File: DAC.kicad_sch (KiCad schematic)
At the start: 0 parts

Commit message: Connected FPGA and DAC
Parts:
- added C64, C65, C66, C67: 10u, symbol Device:C_Polarized_US
- added U8: ~, symbol GuitarZero:PCM1754
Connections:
- new net: C66.1, U8.7 (VoutL)
- new net: C67.1, U8.8 (VoutR)
- new net: C64.1, U8.10 (Vcom)
- new net +5V: C65.1, U8.6 (VCC)
- new net BIT_CLOCK: U8.1 (BCK)
- new net DATA_INN: U8.2 (DATA)
- new net GND: C64.2, C65.2, U8.12 (TEST), U8.13 (DEMP), U8.14 (MUTE), U8.15 (FMT), U8.4 (DGND), U8.9 (AGND)
- new net LEFT_RIGHT_CLOCK: U8.3 (LRCK)
- new net OUT_LEFT: C66.2
- new net OUT_RIGHT: C67.2
- new net SYSTEM_CLOCK_INPUT: U8.16 (SCK)
- no-connect marks 0 -> 2
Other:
- note added: "Theese could be used But would require aditional logic And should be done in the FPGA if needed"

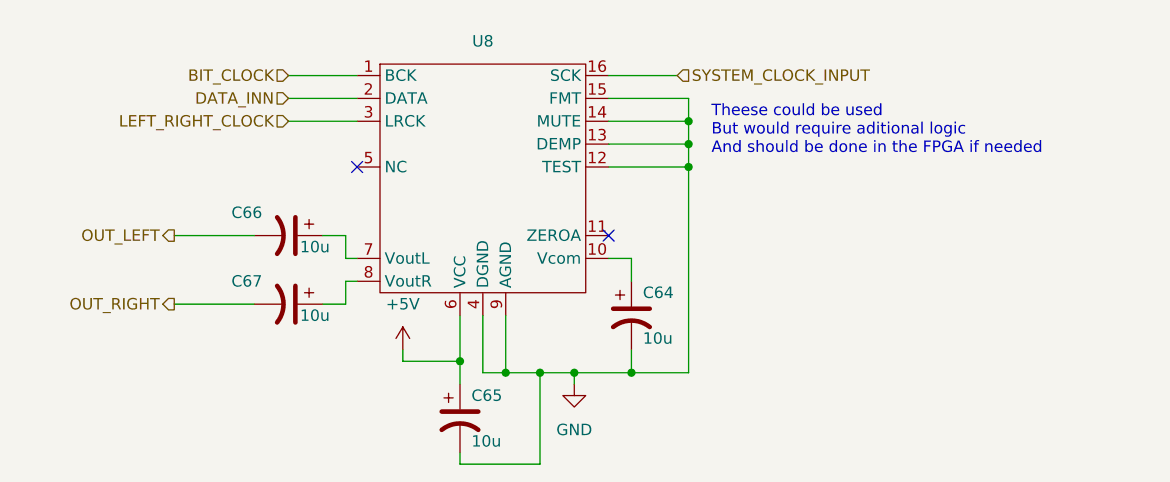
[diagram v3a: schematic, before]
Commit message: Now follows with Electrical Rules
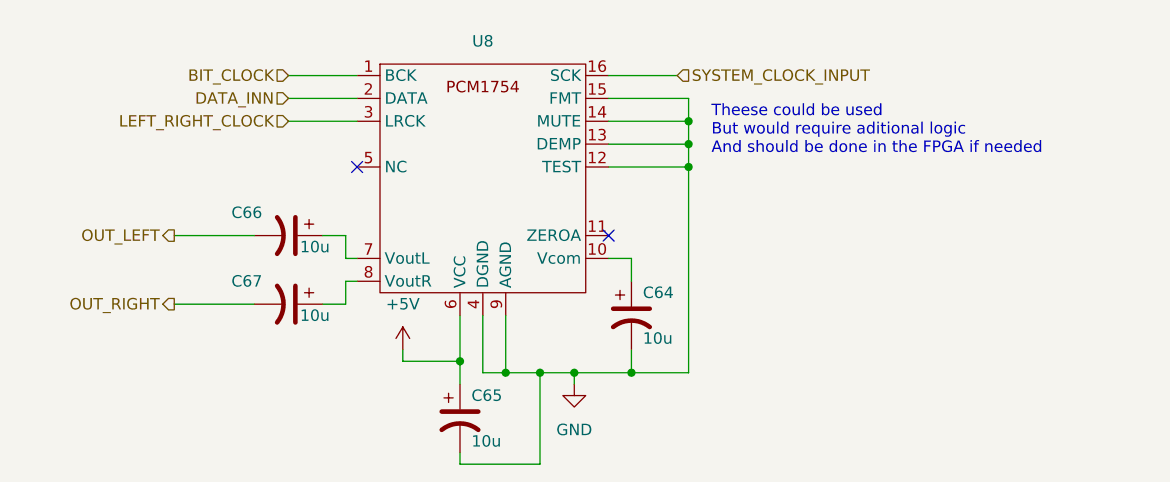
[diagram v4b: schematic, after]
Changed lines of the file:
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@@
     (effects (font (size 1.27 1.27)) (justify left))
+  )
+  (symbol (lib_id "GuitarZero:PCM1754") (at 125.73 92.71 0) (unit 1)
+    (in_bom yes) (on_board yes) (dnp no) (fields_autoplaced)
+    (property "Reference" "U8" (at 125.73 78.74 0)
+      (effects (font (size 1.27 1.27)))
+    )
+    (property "Value" "~" (at 118.11 85.09 0)
+      (effects (font (size 1.27 1.27)))
+    )
+    (property "Footprint" "" (at 118.11 85.09 0)
+      (effects (font (size 1.27 1.27)) hide)
+    )
+    (property "Datasheet" "" (at 118.11 85.09 0)
+      (effects (font (size 1.27 1.27)) hide)
+    )
+    (pin "1")
+    (pin "10")
+    (pin "11")
+    (pin "12")
+    (pin "13")
+    (pin "14")
+    (pin "15")
+    (pin "16")
+    (pin "2")
+    (pin "3")
+    (pin "4")
+    (pin "5")
+    (pin "6")
+    (pin "7")
+    (pin "8")
+    (pin "9")
+    (instances
+      (project "GuitarZero"
+        (path "/fba50eda-8593-4456-af98-ff56fd418a76/17583736-1e43-4d1e-aeda-75c9cd3f21c5"
+          (reference "U8") (unit 1)
+        )
+      )
+    )
   )
   (symbol (lib_id "Device:C_Polarized_US") (at 104.14 100.33 270) (unit 1)
@@
         )
       )
-    )
-  )
-  (symbol (lib_id "GuitarZero:PCM1754") (at 118.11 85.09 0) (unit 1)
-    (in_bom yes) (on_board yes) (dnp no) (fields_autoplaced)
-    (property "Reference" "U8" (at 125.73 78.74 0)
-      (effects (font (size 1.27 1.27)))
-    )
-    (property "Value" "~" (at 118.11 85.09 0)
-      (effects (font (size 1.27 1.27)))
-    )
-    (property "Footprint" "" (at 118.11 85.09 0)
-      (effects (font (size 1.27 1.27)) hide)
-    )
-    (property "Datasheet" "" (at 118.11 85.09 0)
-      (effects (font (size 1.27 1.27)) hide)
-    )
-    (pin "1")
-    (pin "10")
-    (pin "11")
-    (pin "12")
-    (pin "13")
-    (pin "14")
-    (pin "15")
-    (pin "16")
-    (pin "2")
-    (pin "3")
-    (pin "4")
-    (pin "5")
-    (pin "6")
-    (pin "7")
-    (pin "8")
-    (pin "9")
-    (instances
-      (project "GuitarZero"
-        (path "/fba50eda-8593-4456-af98-ff56fd418a76/17583736-1e43-4d1e-aeda-75c9cd3f21c5"
-          (reference "U8") (unit 1)
-        )
-      )

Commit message: Added Anti-noise resistors to DAC
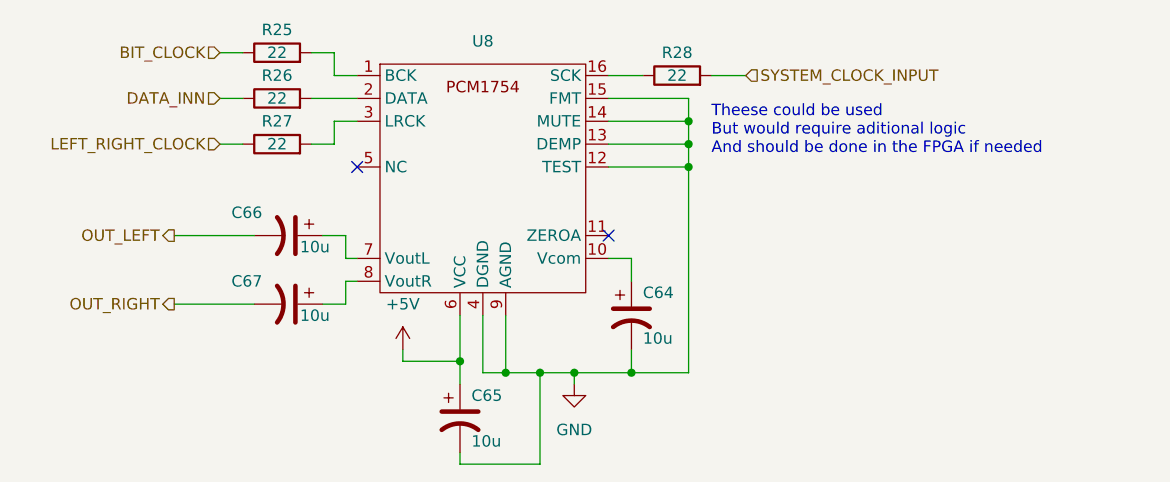
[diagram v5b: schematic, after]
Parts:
- added R25, R26, R27, R28: 22, symbol Device:R
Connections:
- net BIT_CLOCK: now also R25.1; no longer U8.1 (BCK)
- net DATA_INN: now also R26.1; no longer U8.2 (DATA)
- net LEFT_RIGHT_CLOCK: now also R27.1; no longer U8.3 (LRCK)
- net SYSTEM_CLOCK_INPUT: now also R28.2; no longer U8.16 (SCK)
- new net: R25.2, U8.1 (BCK)
- new net: R28.1, U8.16 (SCK)
- new net: R26.2, U8.2 (DATA)
- new net: R27.2, U8.3 (LRCK)
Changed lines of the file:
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@@
-    (stroke (width 0) (type default))
-  )
-  (wire (pts (xy 104.14 85.09) (xy 111.76 85.09))
     (stroke (width 0) (type default))
   )
@@
     (stroke (width 0) (type default))
   )
+  (wire (pts (xy 109.22 80.01) (xy 109.22 82.55))
+    (stroke (width 0) (type default))
+  )
   (wire (pts (xy 132.08 125.73) (xy 132.08 115.57))
     (stroke (width 0) (type default))
   )
+  (wire (pts (xy 96.52 80.01) (xy 99.06 80.01))
+    (stroke (width 0) (type default))
+  )
   (wire (pts (xy 148.59 115.57) (xy 142.24 115.57))
     (stroke (width 0) (type default))
@@
     (stroke (width 0) (type default))
   )
+  (wire (pts (xy 106.68 90.17) (xy 109.22 90.17))
+    (stroke (width 0) (type default))
+  )
+  (wire (pts (xy 139.7 82.55) (xy 143.51 82.55))
+    (stroke (width 0) (type default))
+  )
   (wire (pts (xy 139.7 90.17) (xy 148.59 90.17))
     (stroke (width 0) (type default))
   )
+  (wire (pts (xy 109.22 90.17) (xy 109.22 87.63))
+    (stroke (width 0) (type default))
+  )
   (wire (pts (xy 148.59 90.17) (xy 148.59 92.71))
     (stroke (width 0) (type default))
@@
     (stroke (width 0) (type default))
   )
-  (wire (pts (xy 104.14 82.55) (xy 111.76 82.55))
-    (stroke (width 0) (type default))
-  )
   (wire (pts (xy 148.59 87.63) (xy 148.59 90.17))
     (stroke (width 0) (type default))
   )
+  (wire (pts (xy 106.68 85.09) (xy 111.76 85.09))
+    (stroke (width 0) (type default))
+  )
   (wire (pts (xy 128.27 115.57) (xy 132.08 115.57))
     (stroke (width 0) (type default))
@@
     (stroke (width 0) (type default))
   )
+  (wire (pts (xy 109.22 82.55) (xy 111.76 82.55))
+    (stroke (width 0) (type default))
+  )
   (wire (pts (xy 142.24 102.87) (xy 139.7 102.87))
     (stroke (width 0) (type default))
@@
     (stroke (width 0) (type default))
   )
-  (wire (pts (xy 139.7 82.55) (xy 147.32 82.55))
-    (stroke (width 0) (type default))
-  )
   (wire (pts (xy 128.27 109.22) (xy 128.27 115.57))
     (stroke (width 0) (type default))
@@
     (stroke (width 0) (type default))
   )
+  (wire (pts (xy 109.22 87.63) (xy 111.76 87.63))
+    (stroke (width 0) (type default))
+  )
   (wire (pts (xy 91.44 107.95) (xy 100.33 107.95))
     (stroke (width 0) (type default))
@@
     (stroke (width 0) (type default))
   )
+  (wire (pts (xy 106.68 80.01) (xy 109.22 80.01))
+    (stroke (width 0) (type default))
+  )
+  (wire (pts (xy 96.52 85.09) (xy 99.06 85.09))
+    (stroke (width 0) (type default))
+  )
   (wire (pts (xy 123.19 109.22) (xy 123.19 114.3))
     (stroke (width 0) (type default))
   )
-  (wire (pts (xy 104.14 87.63) (xy 111.76 87.63))
+  (wire (pts (xy 96.52 90.17) (xy 99.06 90.17))
     (stroke (width 0) (type default))
   )
@@
   )
   (wire (pts (xy 110.49 105.41) (xy 110.49 107.95))
+    (stroke (width 0) (type default))
+  )
+  (wire (pts (xy 151.13 82.55) (xy 154.94 82.55))
     (stroke (width 0) (type default))
   )
@@
     (effects (font (size 1.27 1.27)) (justify left bottom))
   )
-  (hierarchical_label "LEFT_RIGHT_CLOCK" (shape input) (at 104.14 87.63 180) (fields_autoplaced)
+  (hierarchical_label "LEFT_RIGHT_CLOCK" (shape input) (at 96.52 90.17 180) (fields_autoplaced)
     (effects (font (size 1.27 1.27)) (justify right))
   )
@@
     (effects (font (size 1.27 1.27)) (justify right))
   )
-  (hierarchical_label "DATA_INN" (shape input) (at 104.14 85.09 180) (fields_autoplaced)
+  (hierarchical_label "DATA_INN" (shape input) (at 96.52 85.09 180) (fields_autoplaced)
     (effects (font (size 1.27 1.27)) (justify right))
   )
@@
     (effects (font (size 1.27 1.27)) (justify right))
   )
-  (hierarchical_label "BIT_CLOCK" (shape input) (at 104.14 82.55 180) (fields_autoplaced)
+  (hierarchical_label "BIT_CLOCK" (shape input) (at 96.52 80.01 180) (fields_autoplaced)
     (effects (font (size 1.27 1.27)) (justify right))
   )
-  (hierarchical_label "SYSTEM_CLOCK_INPUT" (shape input) (at 147.32 82.55 0) (fields_autoplaced)
+  (hierarchical_label "SYSTEM_CLOCK_INPUT" (shape input) (at 154.94 82.55 0) (fields_autoplaced)
     (effects (font (size 1.27 1.27)) (justify left))
+  )
+  (symbol (lib_id "Device:R") (at 102.87 80.01 90) (unit 1)
+    (in_bom yes) (on_board yes) (dnp no)
+    (property "Reference" "R25" (at 102.87 77.47 90)
+      (effects (font (size 1.27 1.27)))
+    )
+    (property "Value" "22" (at 102.87 80.01 90)
+      (effects (font (size 1.27 1.27)))
+    )
+    (property "Footprint" "" (at 102.87 81.788 90)
+      (effects (font (size 1.27 1.27)) hide)
+    )
+    (property "Datasheet" "~" (at 102.87 80.01 0)
+      (effects (font (size 1.27 1.27)) hide)
+    )
+    (pin "1")
+    (pin "2")
+    (instances
+      (project "GuitarZero"
+        (path "/fba50eda-8593-4456-af98-ff56fd418a76/17583736-1e43-4d1e-aeda-75c9cd3f21c5"
+          (reference "R25") (unit 1)
+        )
+      )
+    )
   )
   (symbol (lib_id "GuitarZero:PCM1754") (at 125.73 92.71 0) (unit 1)
@@
     )
   )
+  (symbol (lib_id "Device:R") (at 147.32 82.55 90) (unit 1)
+    (in_bom yes) (on_board yes) (dnp no)
+    (property "Reference" "R28" (at 147.32 80.01 90)
+      (effects (font (size 1.27 1.27)))
+    )
+    (property "Value" "22" (at 147.32 82.55 90)
+      (effects (font (size 1.27 1.27)))
+    )
+    (property "Footprint" "" (at 147.32 84.328 90)
+      (effects (font (size 1.27 1.27)) hide)
+    )
+    (property "Datasheet" "~" (at 147.32 82.55 0)
+      (effects (font (size 1.27 1.27)) hide)
+    )
+    (pin "1")
+    (pin "2")
+    (instances
+      (project "GuitarZero"
+        (path "/fba50eda-8593-4456-af98-ff56fd418a76/17583736-1e43-4d1e-aeda-75c9cd3f21c5"
+          (reference "R28") (unit 1)
+        )
+      )
+    )
+  )
+  (symbol (lib_id "Device:R") (at 102.87 85.09 90) (unit 1)
+    (in_bom yes) (on_board yes) (dnp no)
+    (property "Reference" "R26" (at 102.87 82.55 90)
+      (effects (font (size 1.27 1.27)))
+    )
+    (property "Value" "22" (at 102.87 85.09 90)
+      (effects (font (size 1.27 1.27)))
+    )
+    (property "Footprint" "" (at 102.87 86.868 90)
+      (effects (font (size 1.27 1.27)) hide)
+    )
+    (property "Datasheet" "~" (at 102.87 85.09 0)
+      (effects (font (size 1.27 1.27)) hide)
+    )
+    (pin "1")
+    (pin "2")
+    (instances
+      (project "GuitarZero"
+        (path "/fba50eda-8593-4456-af98-ff56fd418a76/17583736-1e43-4d1e-aeda-75c9cd3f21c5"
+          (reference "R26") (unit 1)
+        )
+      )
+    )
+  )
   (symbol (lib_id "Device:C_Polarized_US") (at 142.24 109.22 0) (unit 1)
     (in_bom yes) (on_board yes) (dnp no)
@@
         )
       )
+    )
+  )
+  (symbol (lib_id "Device:R") (at 102.87 90.17 90) (unit 1)
+    (in_bom yes) (on_board yes) (dnp no)
+    (property "Reference" "R27" (at 102.87 87.63 90)
+      (effects (font (size 1.27 1.27)))
+    )
+    (property "Value" "22" (at 102.87 90.17 90)
+      (effects (font (size 1.27 1.27)))
+    )
+    (property "Footprint" "" (at 102.87 91.948 90)
+      (effects (font (size 1.27 1.27)) hide)
+    )
+    (property "Datasheet" "~" (at 102.87 90.17 0)
+      (effects (font (size 1.27 1.27)) hide)
+    )
+    (pin "1")
+    (pin "2")
+    (instances
+      (project "GuitarZero"
+        (path "/fba50eda-8593-4456-af98-ff56fd418a76/17583736-1e43-4d1e-aeda-75c9cd3f21c5"
+          (reference "R27") (unit 1)
+        )
+      )

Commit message: Added footprints to symbols
Some nice light work
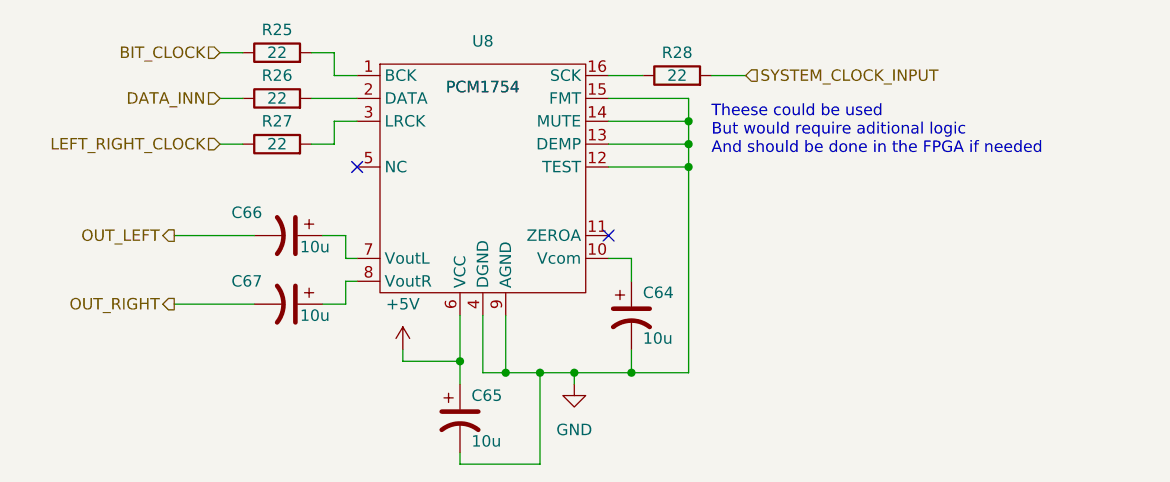
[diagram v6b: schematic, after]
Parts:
- C64, C65, C66, C67: footprint (none) -> Capacitor_SMD:C_1206_3216Metric
- R25, R26, R27, R28: footprint (none) -> Resistor_SMD:R_1206_3216Metric
- U8: value ~ -> PCM1754; footprint (none) -> PCM1754DBQR:SOP63P599X175-16N
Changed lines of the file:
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@@
       (effects (font (size 1.27 1.27)))
     )
-    (property "Footprint" "" (at 102.87 81.788 90)
+    (property "Footprint" "Resistor_SMD:R_1206_3216Metric" (at 102.87 81.788 90)
       (effects (font (size 1.27 1.27)) hide)
     )
@@
   )
   (symbol (lib_id "GuitarZero:PCM1754") (at 125.73 92.71 0) (unit 1)
-    (in_bom yes) (on_board yes) (dnp no) (fields_autoplaced)
+    (in_bom yes) (on_board yes) (dnp no)
     (property "Reference" "U8" (at 125.73 78.74 0)
       (effects (font (size 1.27 1.27)))
     )
-    (property "Value" "~" (at 118.11 85.09 0)
-      (effects (font (size 1.27 1.27)))
-    )
-    (property "Footprint" "" (at 118.11 85.09 0)
+    (property "Value" "PCM1754" (at 125.73 83.82 0)
+      (effects (font (size 1.27 1.27)))
+    )
+    (property "Footprint" "PCM1754DBQR:SOP63P599X175-16N" (at 118.11 85.09 0)
       (effects (font (size 1.27 1.27)) hide)
     )
@@
       (effects (font (size 1.27 1.27)) (justify left))
     )
-    (property "Footprint" "" (at 104.14 100.33 0)
+    (property "Footprint" "Capacitor_SMD:C_1206_3216Metric" (at 104.14 100.33 0)
       (effects (font (size 1.27 1.27)) hide)
     )
@@
       (effects (font (size 1.27 1.27)) (justify left))
     )
-    (property "Footprint" "" (at 104.14 107.95 0)
+    (property "Footprint" "Capacitor_SMD:C_1206_3216Metric" (at 104.14 107.95 0)
       (effects (font (size 1.27 1.27)) hide)
     )
@@
       (effects (font (size 1.27 1.27)))
     )
-    (property "Footprint" "" (at 147.32 84.328 90)
+    (property "Footprint" "Resistor_SMD:R_1206_3216Metric" (at 147.32 84.328 90)
       (effects (font (size 1.27 1.27)) hide)
     )
@@
       (effects (font (size 1.27 1.27)))
     )
-    (property "Footprint" "" (at 102.87 86.868 90)
+    (property "Footprint" "Resistor_SMD:R_1206_3216Metric" (at 102.87 86.868 90)
       (effects (font (size 1.27 1.27)) hide)
     )
@@
       (effects (font (size 1.27 1.27)) (justify left))
     )
-    (property "Footprint" "" (at 142.24 109.22 0)
+    (property "Footprint" "Capacitor_SMD:C_1206_3216Metric" (at 142.24 109.22 0)
       (effects (font (size 1.27 1.27)) hide)
     )
@@
       (effects (font (size 1.27 1.27)))
     )
-    (property "Footprint" "" (at 102.87 91.948 90)
+    (property "Footprint" "Resistor_SMD:R_1206_3216Metric" (at 102.87 91.948 90)
       (effects (font (size 1.27 1.27)) hide)
     )
@@
       (effects (font (size 1.27 1.27)) (justify left))
     )
-    (property "Footprint" "" (at 123.19 120.65 0)
-      (effects (font (size 1.27 1.27)) hide)
-    )
+    (property "Footprint" "Capacitor_SMD:C_1206_3216Metric" (at 123.19 120.65 0)
+      (effects (font (size 1.27 1.27)) hide)
+    )

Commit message: Changed Reistor and Capacitor size fomr 1206 to 0805
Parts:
- C64, C65, C66, C67: footprint Capacitor_SMD:C_1206_3216Metric -> Capacitor_SMD:C_0805_2012Metric
- R25, R26, R27, R28: footprint Resistor_SMD:R_1206_3216Metric -> Resistor_SMD:R_0805_2012Metric
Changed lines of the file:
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@@
       (effects (font (size 1.27 1.27)))
     )
-    (property "Footprint" "Resistor_SMD:R_1206_3216Metric" (at 102.87 81.788 90)
+    (property "Footprint" "Resistor_SMD:R_0805_2012Metric" (at 102.87 81.788 90)
       (effects (font (size 1.27 1.27)) hide)
     )
@@
       (effects (font (size 1.27 1.27)) (justify left))
     )
-    (property "Footprint" "Capacitor_SMD:C_1206_3216Metric" (at 104.14 100.33 0)
+    (property "Footprint" "Capacitor_SMD:C_0805_2012Metric" (at 104.14 100.33 0)
       (effects (font (size 1.27 1.27)) hide)
     )
@@
       (effects (font (size 1.27 1.27)) (justify left))
     )
-    (property "Footprint" "Capacitor_SMD:C_1206_3216Metric" (at 104.14 107.95 0)
+    (property "Footprint" "Capacitor_SMD:C_0805_2012Metric" (at 104.14 107.95 0)
       (effects (font (size 1.27 1.27)) hide)
     )
@@
       (effects (font (size 1.27 1.27)))
     )
-    (property "Footprint" "Resistor_SMD:R_1206_3216Metric" (at 147.32 84.328 90)
+    (property "Footprint" "Resistor_SMD:R_0805_2012Metric" (at 147.32 84.328 90)
       (effects (font (size 1.27 1.27)) hide)
     )
@@
       (effects (font (size 1.27 1.27)))
     )
-    (property "Footprint" "Resistor_SMD:R_1206_3216Metric" (at 102.87 86.868 90)
+    (property "Footprint" "Resistor_SMD:R_0805_2012Metric" (at 102.87 86.868 90)
       (effects (font (size 1.27 1.27)) hide)
     )
@@
       (effects (font (size 1.27 1.27)) (justify left))
     )
-    (property "Footprint" "Capacitor_SMD:C_1206_3216Metric" (at 142.24 109.22 0)
+    (property "Footprint" "Capacitor_SMD:C_0805_2012Metric" (at 142.24 109.22 0)
       (effects (font (size 1.27 1.27)) hide)
     )
@@
       (effects (font (size 1.27 1.27)))
     )
-    (property "Footprint" "Resistor_SMD:R_1206_3216Metric" (at 102.87 91.948 90)
+    (property "Footprint" "Resistor_SMD:R_0805_2012Metric" (at 102.87 91.948 90)
       (effects (font (size 1.27 1.27)) hide)
     )
@@
       (effects (font (size 1.27 1.27)) (justify left))
     )
-    (property "Footprint" "Capacitor_SMD:C_1206_3216Metric" (at 123.19 120.65 0)
-      (effects (font (size 1.27 1.27)) hide)
-    )
+    (property "Footprint" "Capacitor_SMD:C_0805_2012Metric" (at 123.19 120.65 0)
+      (effects (font (size 1.27 1.27)) hide)
+    )
